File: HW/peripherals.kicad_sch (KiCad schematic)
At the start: 17 parts, among them J4 USB_C_Receptacle_USB2.0, J5 OLED, Q2 BC817, Q3 BC817, SW1 SW_SPST, SW4 SW_SPST, SW5 SW_SPST, U3 CH340C

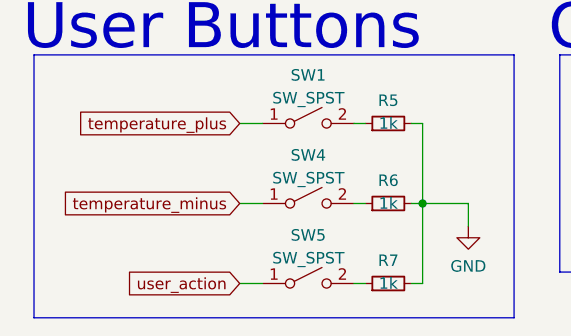
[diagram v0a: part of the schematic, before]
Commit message: Finished routing, only mosfet left, fixed layout, outline
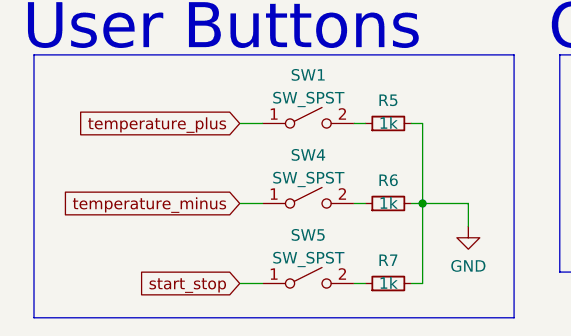
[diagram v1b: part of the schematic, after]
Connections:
- net user_action renamed start_stop
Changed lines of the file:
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@@
     )
   )
-  (global_label "user_action" (shape input) (at 54.61 139.7 180) (fields_autoplaced)
+  (global_label "start_stop" (shape input) (at 54.61 139.7 180) (fields_autoplaced)
     (effects (font (size 1.27 1.27)) (justify right))
-    (property "Intersheet References" "${INTERSHEET_REFS}" (id 0) (at 41.3112 139.6206 0)
+    (property "Intersheet References" "${INTERSHEET_REFS}" (id 0) (at 42.7626 139.6206 0)
       (effects (font (size 1.27 1.27)) (justify right) hide)
     )

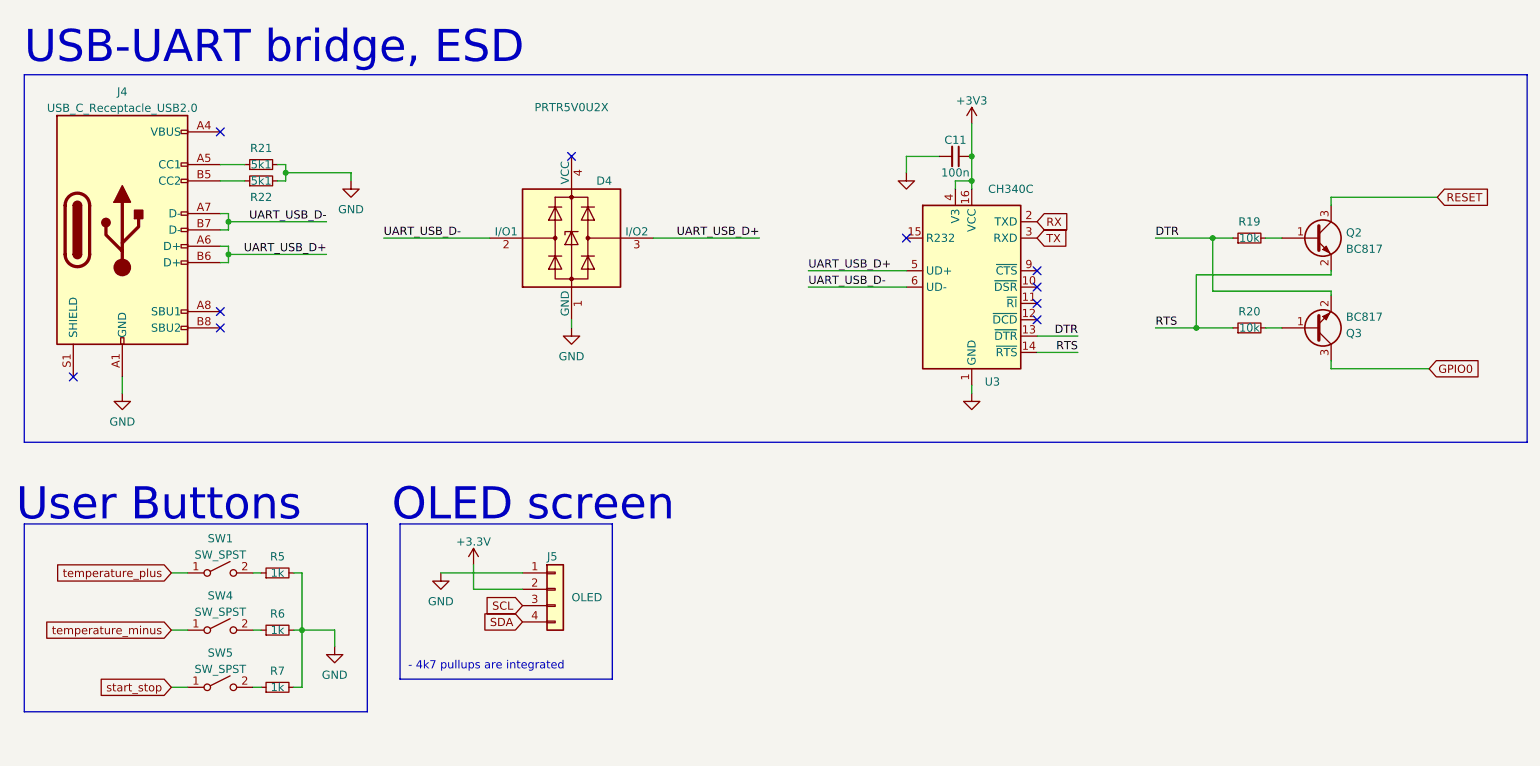
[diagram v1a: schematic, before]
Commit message: QOL changes on pcb, fixed wrong ACDC brick polarity xD
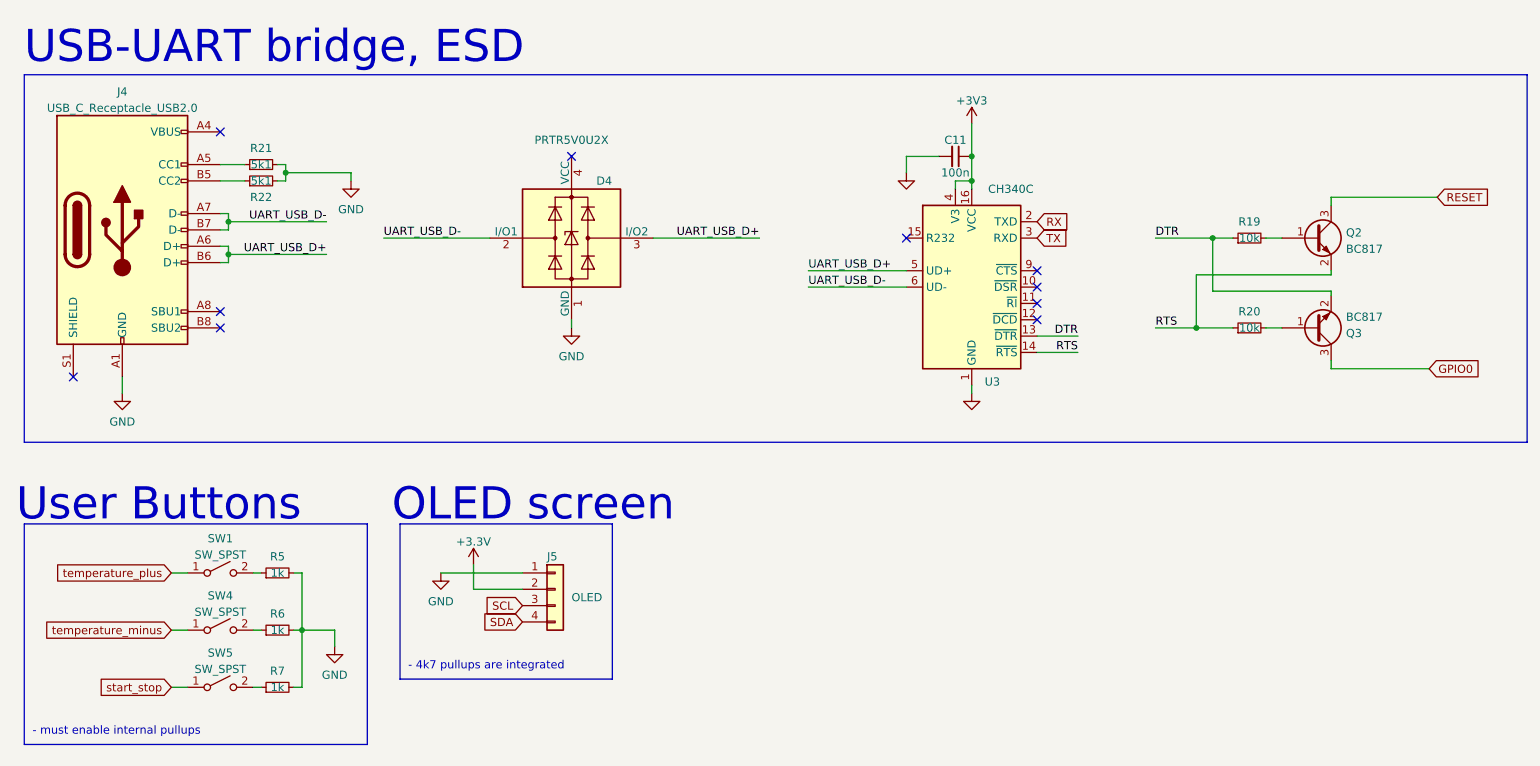
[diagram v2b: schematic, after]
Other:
- note added: "- must enable internal pullups"
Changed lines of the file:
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@@
     (stroke (width 0) (type default) (color 0 0 0 0))
   )
-  (polyline (pts (xy 85.09 143.51) (xy 85.09 114.3))
+  (polyline (pts (xy 85.09 148.59) (xy 85.09 114.3))
     (stroke (width 0) (type default) (color 0 0 0 0))
   )
@@
     (stroke (width 0) (type default) (color 0 0 0 0))
   )
-  (polyline (pts (xy 31.75 143.51) (xy 85.09 143.51))
+  (polyline (pts (xy 31.75 148.59) (xy 85.09 148.59))
     (stroke (width 0) (type default) (color 0 0 0 0))
   )
@@
     (stroke (width 0) (type default) (color 0 0 0 0))
   )
-  (polyline (pts (xy 31.75 114.3) (xy 31.75 143.51))
+  (polyline (pts (xy 31.75 114.3) (xy 31.75 148.59))
     (stroke (width 0) (type default) (color 0 0 0 0))
   )
@@
   (text "USB-UART bridge, ESD" (at 31.75 43.18 0)
     (effects (font (size 5 5)) (justify left bottom))
+  )
+  (text "- must enable internal pullups" (at 33.02 147.32 0)
+    (effects (font (size 1.27 1.27)) (justify left bottom))
   )
   (label "DTR" (at 207.645 69.85 0)
@@
     (in_bom yes) (on_board yes)
     (property "Reference" "D4" (id 0) (at 121.92 60.96 0))
-    (property "Value" "PRTR5V0U2X" (id 1) (at 116.84 49.53 0))
+    (property "Value" "PRTR5V0U2X" (id 1) (at 116.84 54.61 0))
     (property "Footprint" "Package_TO_SOT_SMD:SOT-143" (id 2) (at 118.364 69.85 0)
       (effects (font (size 1.27 1.27)) hide)

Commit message: Fixed silkscreen, removed one thermistor, fixed component placement
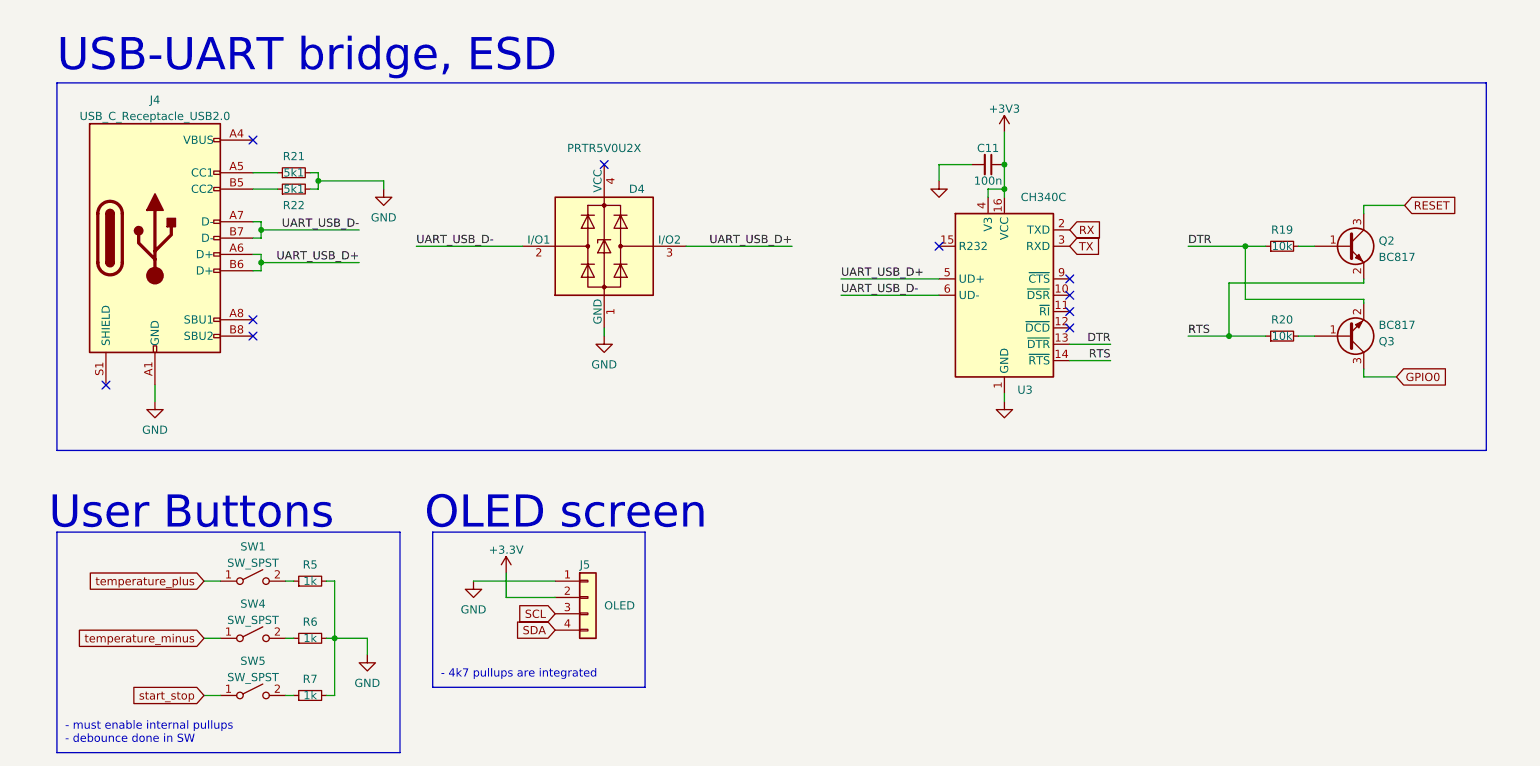
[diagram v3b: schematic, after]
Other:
- note added: "- must enable internal pullups - debounce done in SW"
- note removed: "- must enable internal pullups"
- moved on the sheet: C11, D4, J4, J5, Q2, Q3, R19, R20, R21, R22, R5, R6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
